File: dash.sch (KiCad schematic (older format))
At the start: 24 parts

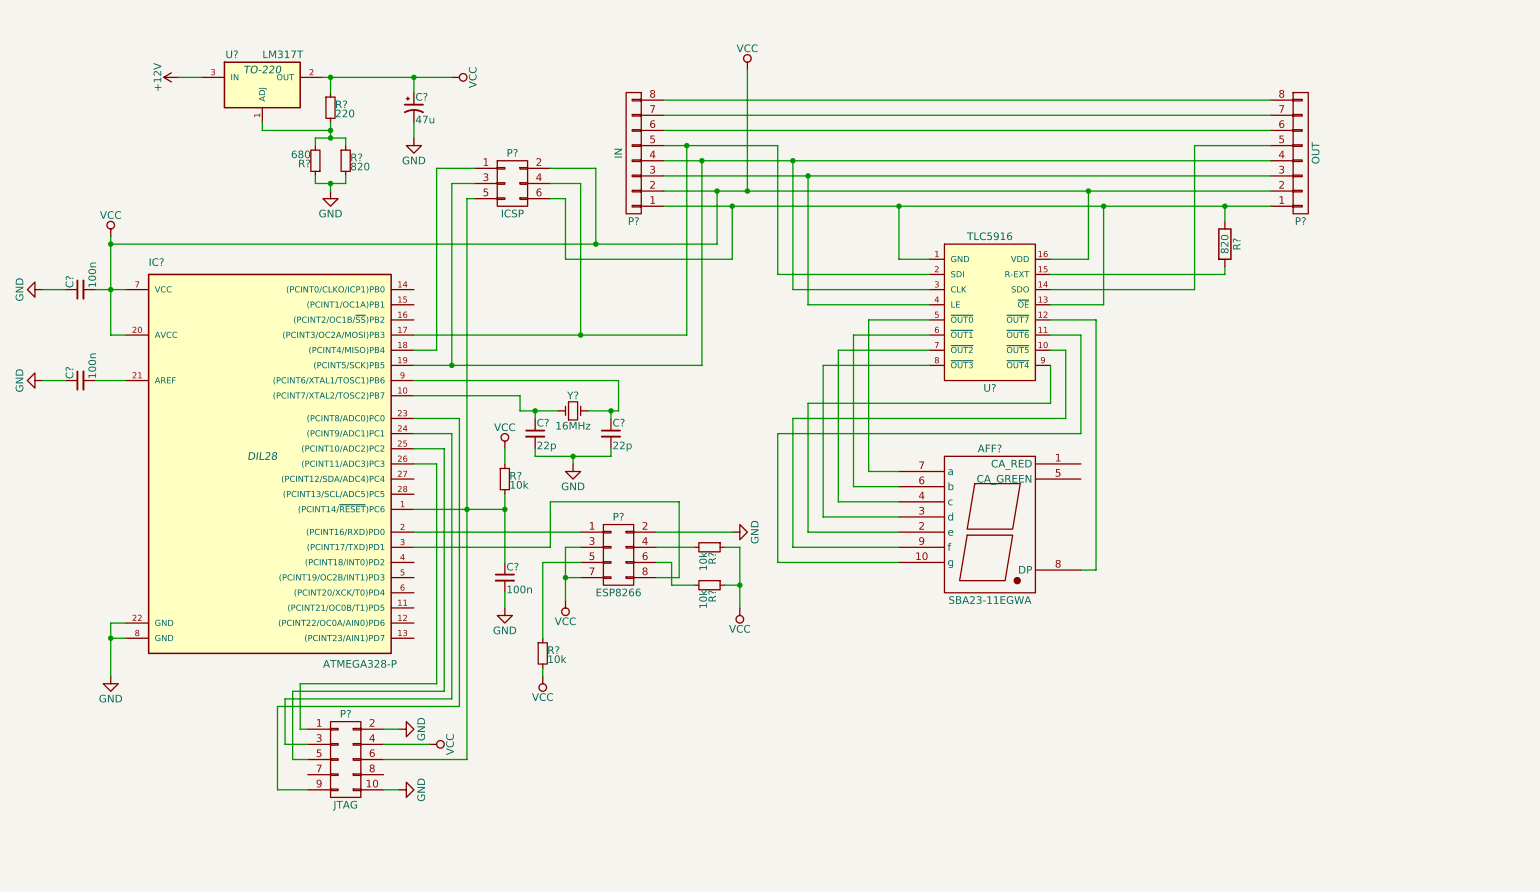
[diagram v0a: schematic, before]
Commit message: Start doing footprint assoc.
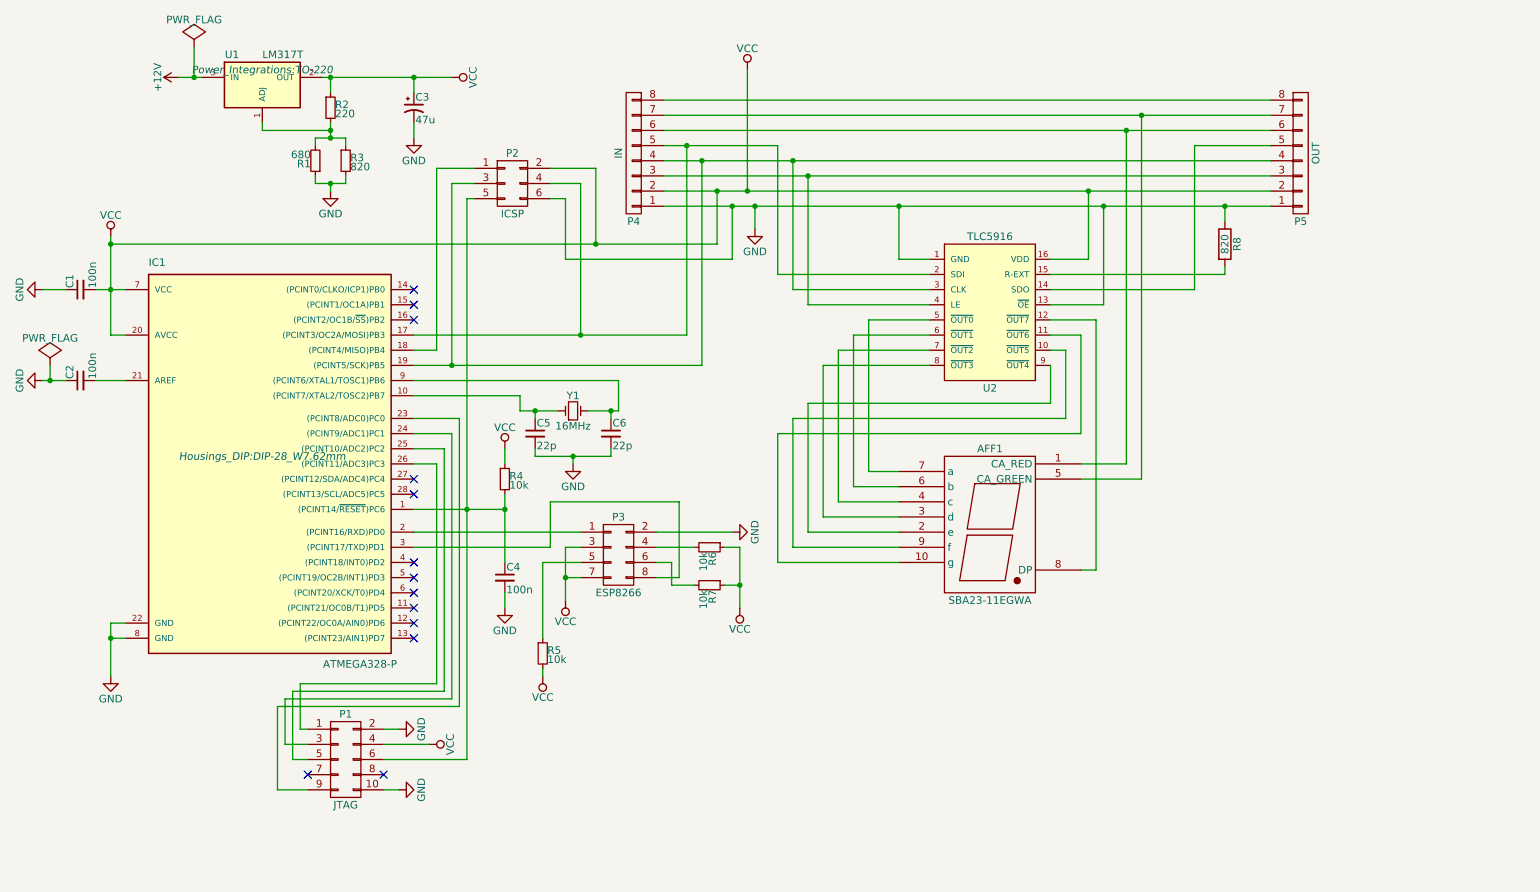
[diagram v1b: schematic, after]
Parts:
- IC1: renamed from IC?; footprint DIL28 -> Housings_DIP:DIP-28_W7.62mm
- P1: renamed from P?; footprint (none) -> Pin_Headers:Pin_Header_Straight_2x05
- P2: renamed from P?; footprint (none) -> Pin_Headers:Pin_Header_Straight_2x03
- P3: renamed from P?; footprint (none) -> Socket_Strips:Socket_Strip_Straight_2x04
- P4: renamed from P?; footprint (none) -> Pin_Headers:Pin_Header_Angled_1x08
- P5: renamed from P?; footprint (none) -> Socket_Strips:Socket_Strip_Angled_1x08
- R1, R2, R3, R4, R5, R6, R7, R8: renamed from R?; footprint (none) -> Resistors_ThroughHole:Resistor_Horizontal_RM7mm
- U1: renamed from U?; footprint TO-220 -> Power_Integrations:TO-220
- U2: renamed from U?; footprint (none) -> Housings_SOIC:SOIC-16_3.9x9.9mm_Pitch1.27mm
- gave numbers to parts that had none: 8
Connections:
- net GND: now also P2.6 (P6), P4.1 (P1), P5.1 (P1), R8.1, U2.1 (GND), U2.13 (~OE)
- net at AFF1.1 (CA_RED): now also P4.6 (P6), P5.6 (P6)
- net at AFF1.5 (CA_GREEN): now also P4.7 (P7), P5.7 (P7)
- no-connect marks 0 -> 13

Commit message: Start some hand-routing.
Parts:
- AFF1: footprint (none) -> redgreen-segment:7SegmentLED_SBA23-11EGWA
- C1, C2, C4, C5, C6: footprint (none) -> Capacitors_SMD:C_0805_HandSoldering
- C3: footprint (none) -> Capacitors_ThroughHole:C_Radial_D5_L11_P2
- R1, R2, R3, R4, R5, R6, R7, R8: footprint Resistors_ThroughHole:Resistor_Horizontal_RM7mm -> Resistors_ThroughHole:Resistor_Horizontal_RM15mm
- Y1: footprint (none) -> Crystals:Crystal_HC49-U_Vertical
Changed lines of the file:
@@
 F 0 "AFF1" H 7100 4850 50  0000 C CNN
 F 1 "SBA23-11EGWA" H 7100 3850 50  0000 C CNN
-F 2 "" H 7100 4300 50  0001 C CNN
+F 2 "redgreen-segment:7SegmentLED_SBA23-11EGWA" H 7100 4300 50  0001 C CNN
 F 3 "" H 7100 4300 50  0000 C CNN
 	1    7100 4300
@@
 F 0 "R8" V 8730 2400 50  0000 C CNN
 F 1 "820" V 8650 2400 50  0000 C CNN
-F 2 "Resistors_ThroughHole:Resistor_Horizontal_RM7mm" V 8580 2400 50  0001 C CNN
+F 2 "Resistors_ThroughHole:Resistor_Horizontal_RM15mm" V 8580 2400 50  0001 C CNN
 F 3 "" H 8650 2400 50  0000 C CNN
 	1    8650 2400
@@
 F 0 "Y1" H 4350 3600 50  0000 C CNN
 F 1 "16MHz" H 4350 3400 50  0000 C CNN
-F 2 "" H 4350 3500 50  0001 C CNN
+F 2 "Crystals:Crystal_HC49-U_Vertical" H 4350 3500 50  0001 C CNN
 F 3 "" H 4350 3500 50  0000 C CNN
 	1    4350 3500
@@
 F 0 "C5" H 4110 3720 50  0000 L CNN
 F 1 "22p" H 4110 3570 50  0000 L CNN
-F 2 "" H 4100 3650 50  0001 C CNN
+F 2 "Capacitors_SMD:C_0805_HandSoldering" H 4100 3650 50  0001 C CNN
 F 3 "" H 4100 3650 50  0000 C CNN
 	1    4100 3650
@@
 F 0 "C6" H 4610 3720 50  0000 L CNN
 F 1 "22p" H 4610 3570 50  0000 L CNN
-F 2 "" H 4600 3650 50  0001 C CNN
+F 2 "Capacitors_SMD:C_0805_HandSoldering" H 4600 3650 50  0001 C CNN
 F 3 "" H 4600 3650 50  0000 C CNN
 	1    4600 3650
@@
 F 0 "C2" H 1110 3370 50  0000 L CNN
 F 1 "100n" H 1110 3220 50  0000 L CNN
-F 2 "" H 1100 3300 50  0001 C CNN
+F 2 "Capacitors_SMD:C_0805_HandSoldering" H 1100 3300 50  0001 C CNN
 F 3 "" H 1100 3300 50  0000 C CNN
 	1    1100 3300
@@
 F 0 "C1" H 1110 2770 50  0000 L CNN
 F 1 "100n" H 1110 2620 50  0000 L CNN
-F 2 "" H 1100 2700 50  0001 C CNN
+F 2 "Capacitors_SMD:C_0805_HandSoldering" H 1100 2700 50  0001 C CNN
 F 3 "" H 1100 2700 50  0000 C CNN
 	1    1100 2700
@@
 F 0 "R4" H 3930 3970 50  0000 L CNN
 F 1 "10k" H 3930 3910 50  0000 L CNN
-F 2 "Resistors_ThroughHole:Resistor_Horizontal_RM7mm" H 3900 3950 50  0001 C CNN
+F 2 "Resistors_ThroughHole:Resistor_Horizontal_RM15mm" H 3900 3950 50  0001 C CNN
 F 3 "" H 3900 3950 50  0000 C CNN
 	1    3900 3950
@@
 F 0 "C4" H 3910 4670 50  0000 L CNN
 F 1 "100n" H 3910 4520 50  0000 L CNN
-F 2 "" H 3900 4600 50  0001 C CNN
+F 2 "Capacitors_SMD:C_0805_HandSoldering" H 3900 4600 50  0001 C CNN
 F 3 "" H 3900 4600 50  0000 C CNN
 	1    3900 4600
@@
 F 0 "R6" H 5280 4420 50  0000 L CNN
 F 1 "10k" H 5280 4360 50  0000 L CNN
-F 2 "Resistors_ThroughHole:Resistor_Horizontal_RM7mm" H 5250 4400 50  0001 C CNN
+F 2 "Resistors_ThroughHole:Resistor_Horizontal_RM15mm" H 5250 4400 50  0001 C CNN
 F 3 "" H 5250 4400 50  0000 C CNN
 	1    5250 4400
@@
 F 0 "R7" H 5280 4670 50  0000 L CNN
 F 1 "10k" H 5280 4610 50  0000 L CNN
-F 2 "Resistors_ThroughHole:Resistor_Horizontal_RM7mm" H 5250 4650 50  0001 C CNN
+F 2 "Resistors_ThroughHole:Resistor_Horizontal_RM15mm" H 5250 4650 50  0001 C CNN
 F 3 "" H 5250 4650 50  0000 C CNN
 	1    5250 4650
@@
 F 0 "R5" H 4180 5120 50  0000 L CNN
 F 1 "10k" H 4180 5060 50  0000 L CNN
-F 2 "Resistors_ThroughHole:Resistor_Horizontal_RM7mm" H 4150 5100 50  0001 C CNN
+F 2 "Resistors_ThroughHole:Resistor_Horizontal_RM15mm" H 4150 5100 50  0001 C CNN
 F 3 "" H 4150 5100 50  0000 C CNN
 	1    4150 5100
@@
 F 0 "R2" H 2780 1520 50  0000 L CNN
 F 1 "220" H 2780 1460 50  0000 L CNN
-F 2 "Resistors_ThroughHole:Resistor_Horizontal_RM7mm" H 2750 1500 50  0001 C CNN
+F 2 "Resistors_ThroughHole:Resistor_Horizontal_RM15mm" H 2750 1500 50  0001 C CNN
 F 3 "" H 2750 1500 50  0000 C CNN
 	1    2750 1500
@@
 F 0 "R1" H 2680 1870 50  0000 L CNN
 F 1 "680" H 2680 1810 50  0000 L CNN
-F 2 "Resistors_ThroughHole:Resistor_Horizontal_RM7mm" H 2650 1850 50  0001 C CNN
+F 2 "Resistors_ThroughHole:Resistor_Horizontal_RM15mm" H 2650 1850 50  0001 C CNN
 F 3 "" H 2650 1850 50  0000 C CNN
 	1    2650 1850
@@
 F 0 "R3" H 2880 1870 50  0000 L CNN
 F 1 "820" H 2880 1810 50  0000 L CNN
-F 2 "Resistors_ThroughHole:Resistor_Horizontal_RM7mm" H 2850 1850 50  0001 C CNN
+F 2 "Resistors_ThroughHole:Resistor_Horizontal_RM15mm" H 2850 1850 50  0001 C CNN
 F 3 "" H 2850 1850 50  0000 C CNN
 	1    2850 1850
@@
 F 0 "C3" H 3310 1570 50  0000 L CNN
 F 1 "47u" H 3310 1420 50  0000 L CNN
-F 2 "" H 3300 1500 50  0001 C CNN
+F 2 "Capacitors_ThroughHole:C_Radial_D5_L11_P2" H 3300 1500 50  0001 C CNN
 F 3 "" H 3300 1500 50  0000 C CNN
 	1    3300 1500

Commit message: Finished routing. Still missing connection from +12 to red/green anode.
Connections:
- net at IC1.16 ((PCINT2/OC1B/~SS~)PB2): now also P4.3 (P3), P5.3 (P3), U2.4 (LE)
- no-connect marks 13 -> 12
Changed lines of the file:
@@
 NoConn ~ 3300 2700
 NoConn ~ 3300 2800
-NoConn ~ 3300 2900
 NoConn ~ 3300 3950
 NoConn ~ 3300 4050
@@
 	1    0    0    -1
 $EndComp
+Wire Wire Line
+	3300 2900 5000 2900
+Wire Wire Line
+	5000 2900 5000 1950
+Connection ~ 5000 1950
 $EndSCHEMATC

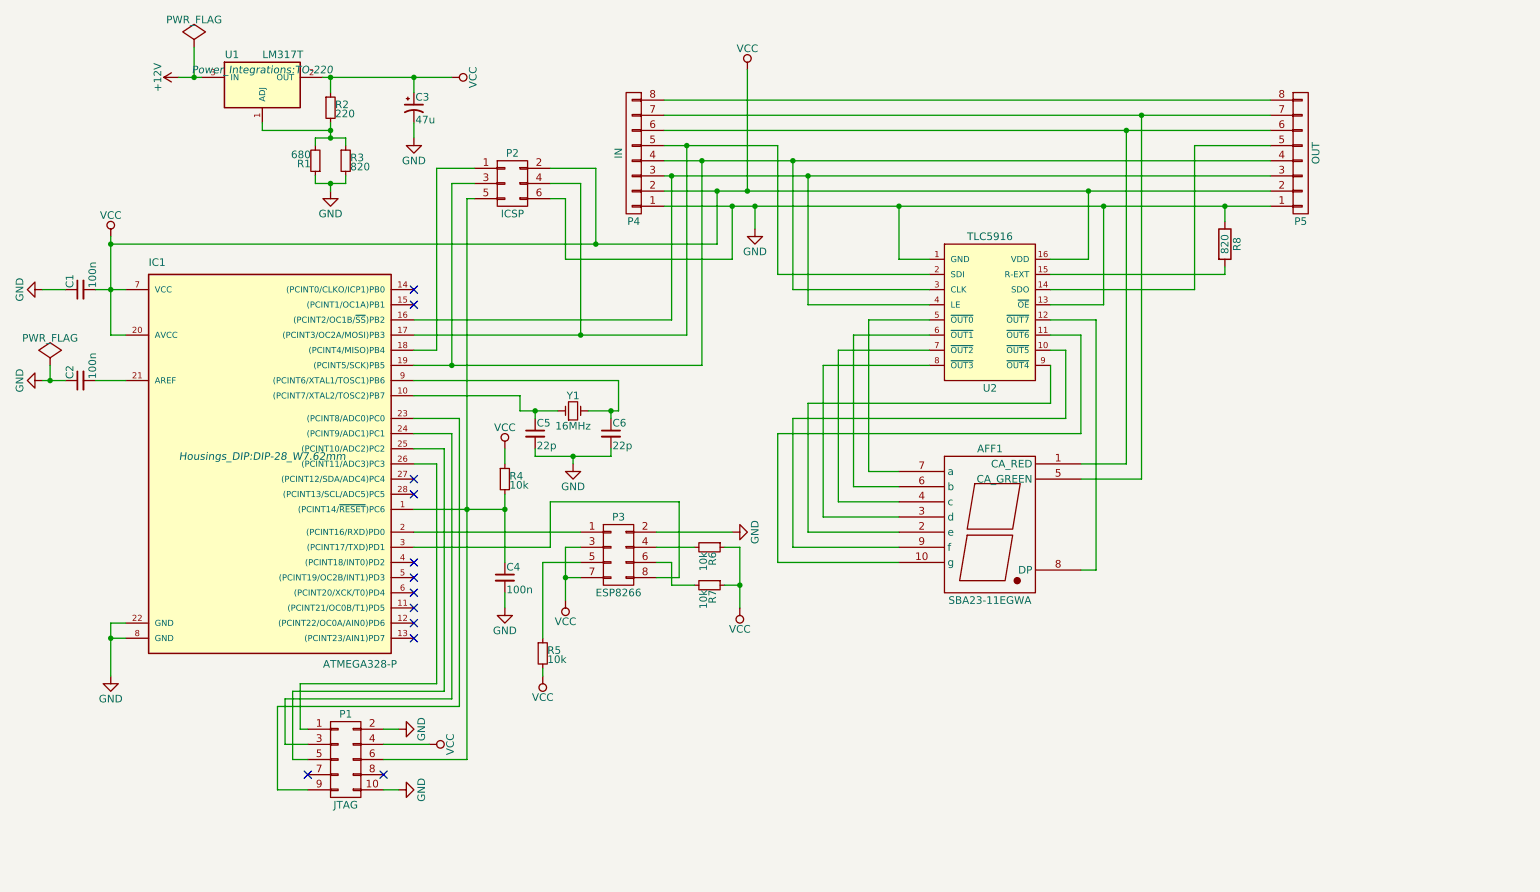
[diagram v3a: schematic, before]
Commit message: Re-layout the PCB. vertical resistors, red/green supply mosfets.
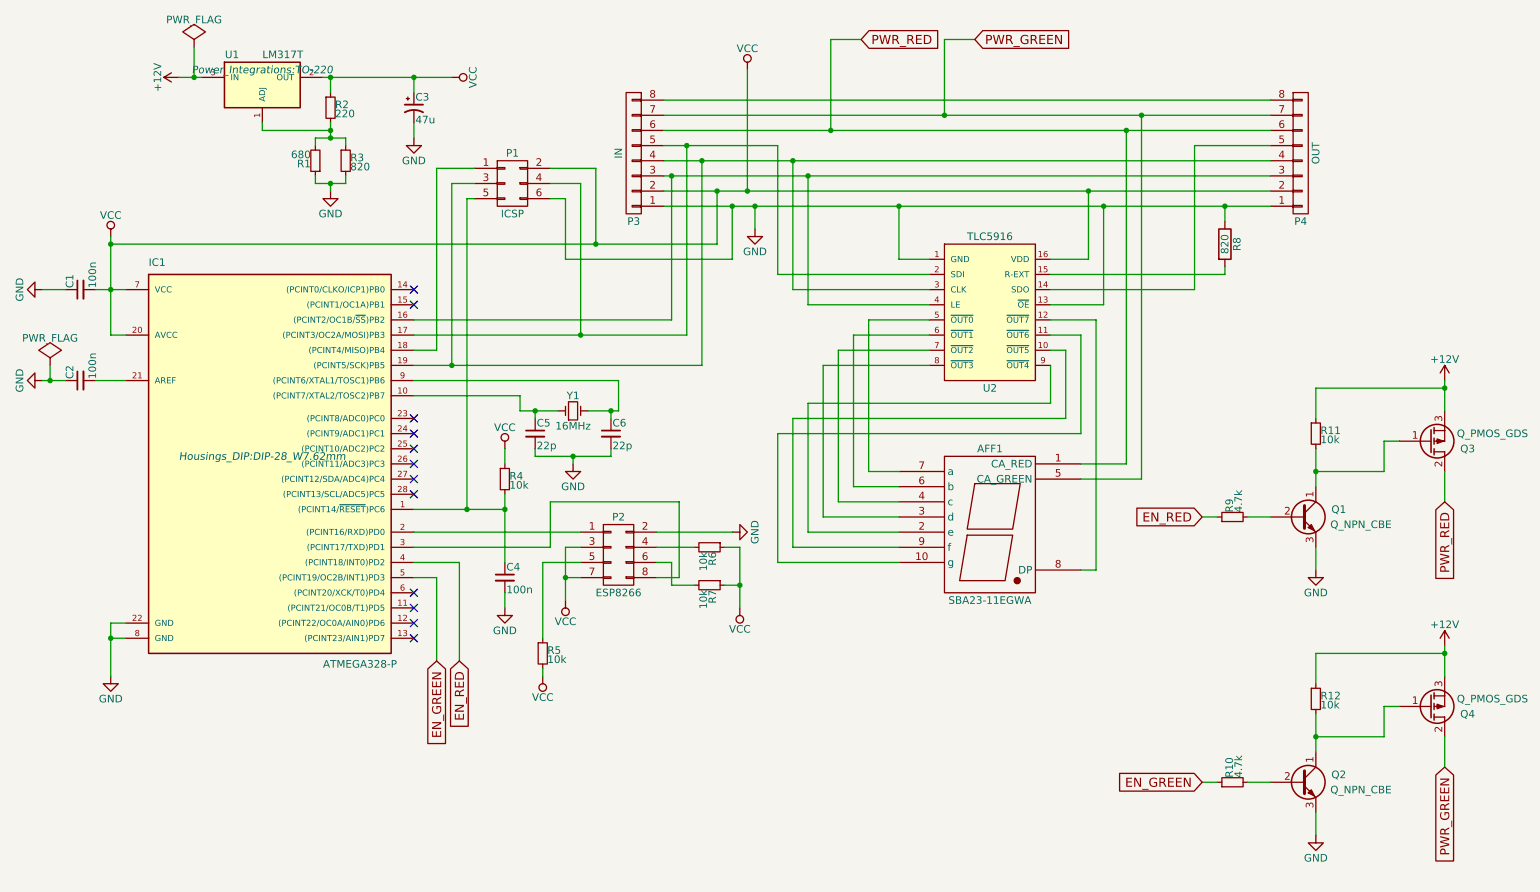
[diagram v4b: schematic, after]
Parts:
- removed P1: JTAG, Pin_Headers:Pin_Header_Straight_2x05, symbol CONN_02X05
- added Q1, Q2: Q_NPN_CBE, TO_SOT_Packages_THT:TO-92_Inline_Narrow_Oval, symbol Q_NPN_CBE
- added Q3, Q4: Q_PMOS_GDS, TO_SOT_Packages_THT:TO-220_Neutral123_Vertical, symbol Q_PMOS_GDS
- added R10, R9: 4.7k, Resistors_ThroughHole:Resistor_Vertical_RM5mm, symbol R_Small
- added R11, R12: 10k, Resistors_ThroughHole:Resistor_Vertical_RM5mm, symbol R_Small
- R1, R2, R3, R4, R5, R6, R7, R8: footprint Resistors_ThroughHole:Resistor_Horizontal_RM15mm -> Resistors_ThroughHole:Resistor_Vertical_RM5mm
- renumbered P2 to P1, P3 to P2, P4 to P3, P5 to P4
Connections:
- net +12V: now also Q3.3 (S), Q4.3 (S), R11.1, R12.1
- net GND: now also Q1.3 (E), Q2.3 (E)
- net EN_RED: now reaches IC1.4 ((PCINT18/INT0)PD2)
- net EN_RED: now also R9.1
- net EN_GREEN: now reaches IC1.5 ((PCINT19/OC2B/INT1)PD3)
- net EN_GREEN: now also R10.1
- net PWR_RED: now reaches AFF1.1 (CA_RED), P3.6 (P6), P4.6 (P6)
- net PWR_RED: now also Q3.2 (D)
- net PWR_GREEN: now reaches AFF1.5 (CA_GREEN), P3.7 (P7), P4.7 (P7)
- net PWR_GREEN: now also Q4.2 (D)
- new net: Q1.1 (C), Q3.1 (G), R11.2
- new net: Q1.2 (B), R9.2
- new net: Q2.1 (C), Q4.1 (G), R12.2
- new net: Q2.2 (B), R10.2

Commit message: Start re-routing new layout.
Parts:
- added P5: DC, Pin_Headers:Pin_Header_Straight_1x02, symbol CONN_01X02
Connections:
- net +12V: now also P5.1 (P1)
- net GND: now also P5.2 (P2)
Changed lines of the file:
@@
 L PWR_FLAG #FLG017
 U 1 1 57938A71
-P 1850 1100
-F 0 "#FLG017" H 1850 1195 50  0001 C CNN
-F 1 "PWR_FLAG" H 1850 1280 50  0000 C CNN
-F 2 "" H 1850 1100 50  0000 C CNN
-F 3 "" H 1850 1100 50  0000 C CNN
-	1    1850 1100
-	1    0    0    -1
-$EndComp
-Wire Wire Line
-	1850 1100 1850 1300
-Connection ~ 1850 1300
+P 10000 1350
+F 0 "#FLG017" H 10000 1445 50  0001 C CNN
+F 1 "PWR_FLAG" H 10000 1530 50  0000 C CNN
+F 2 "" H 10000 1350 50  0000 C CNN
+F 3 "" H 10000 1350 50  0000 C CNN
+	1    10000 1350
+	1    0    0    -1
+$EndComp
 $Comp
 L PWR_FLAG #FLG018
@@
 Wire Wire Line
 	10100 5650 10100 5850
+$Comp
+L CONN_01X02 P5
+U 1 1 57961761
+P 10300 1500
+F 0 "P5" H 10300 1650 50  0000 C CNN
+F 1 "DC" V 10400 1500 50  0000 C CNN
+F 2 "Pin_Headers:Pin_Header_Straight_1x02" H 10300 1500 50  0001 C CNN
+F 3 "" H 10300 1500 50  0000 C CNN
+	1    10300 1500
+	1    0    0    -1
+$EndComp
+$Comp
+L +12V #PWR024
+U 1 1 57961914
+P 9900 1450
+F 0 "#PWR024" H 9900 1300 50  0001 C CNN
+F 1 "+12V" H 9900 1590 50  0000 C CNN
+F 2 "" H 9900 1450 50  0000 C CNN
+F 3 "" H 9900 1450 50  0000 C CNN
+	1    9900 1450
+	0    -1   -1   0
+$EndComp
+Wire Wire Line
+	10100 1450 9900 1450
+Wire Wire Line
+	10000 1350 10000 1450
+Connection ~ 10000 1450
+$Comp
+L GND #PWR025
+U 1 1 57961C93
+P 10000 1650
+F 0 "#PWR025" H 10000 1400 50  0001 C CNN
+F 1 "GND" H 10000 1500 50  0000 C CNN
+F 2 "" H 10000 1650 50  0000 C CNN
+F 3 "" H 10000 1650 50  0000 C CNN
+	1    10000 1650
+	1    0    0    -1
+$EndComp
+Wire Wire Line
+	10100 1550 10000 1550
+Wire Wire Line
+	10000 1550 10000 1650
 $EndSCHEMATC

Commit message: Re-orient the ESP8266 header.
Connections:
- net GND: now also P2.8 (P8); no longer P2.2 (P2)
- net VCC: now also P2.1 (P1), P2.5 (P5); no longer P2.3 (P3), P2.7 (P7)
- net at IC1.2 ((PCINT16/RXD)PD0): now also P2.7 (P7); no longer P2.1 (P1)
- net at IC1.3 ((PCINT17/TXD)PD1): now also P2.2 (P2); no longer P2.8 (P8)
- net at P2.4 (P4): now also R7.2; no longer R6.2
- net at R5.1: now also P2.3 (P3); no longer P2.5 (P5)
- net at P2.6 (P6): now also R6.2; no longer R7.2
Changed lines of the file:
@@
 F 3 "" H 4650 3250 50  0000 C CNN
 	1    4650 4450
-	1    0    0    -1
+	1    0    0    1
 $EndComp
 $Comp
